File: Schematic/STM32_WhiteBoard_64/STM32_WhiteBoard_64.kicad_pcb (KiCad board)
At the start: 2 copper layers, 25.6 x 60.1 mm, 40 parts, among them J1 SWDIO+Serial, J2 USB_B_Micro, J3 Conn_01x22, J4 Conn_01x22, SW1 Boot0, SW2 Reset, U1 STM32F411RET_Arduino, U2 W25Q32JVSSIQ, U4 NCP1117-3.3_SOT223, X1 ASV-8MHz, Y1 ABS25-32.768KHZ-6-T

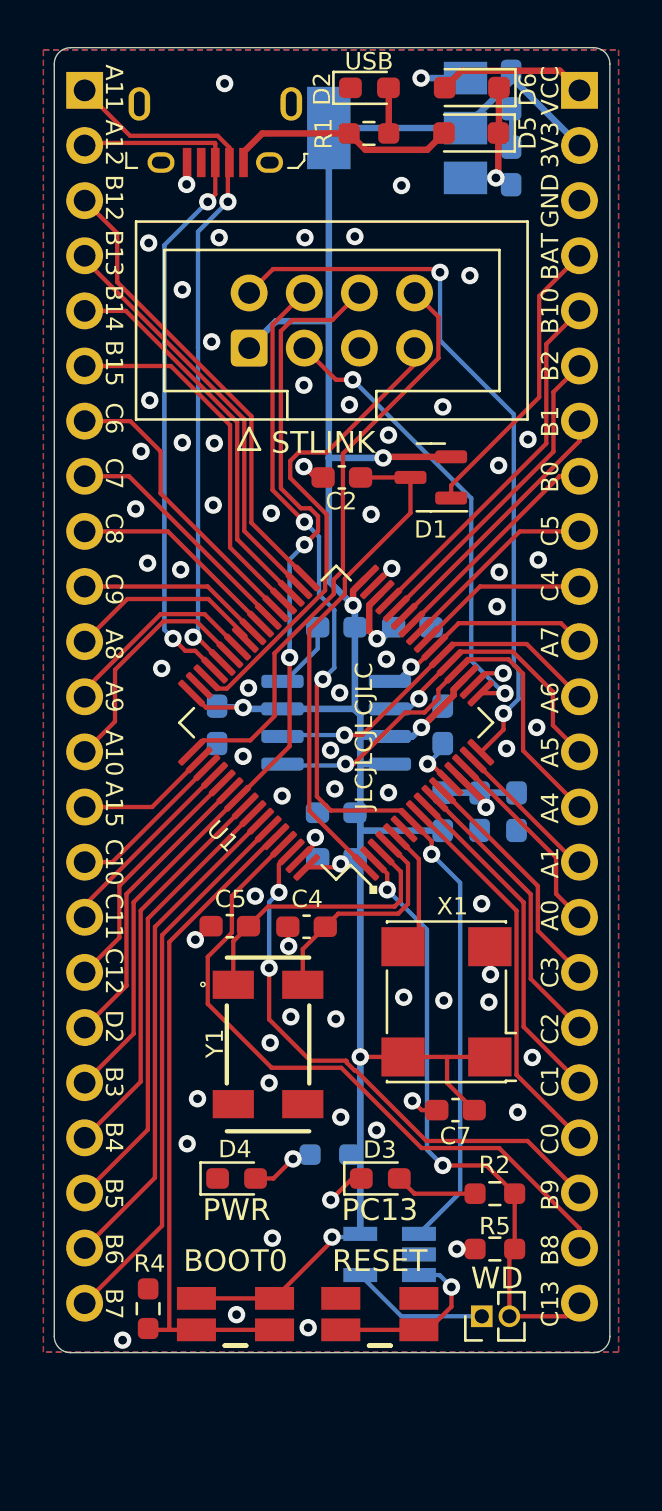
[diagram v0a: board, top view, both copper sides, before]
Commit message: Changed footprints for D6, D7
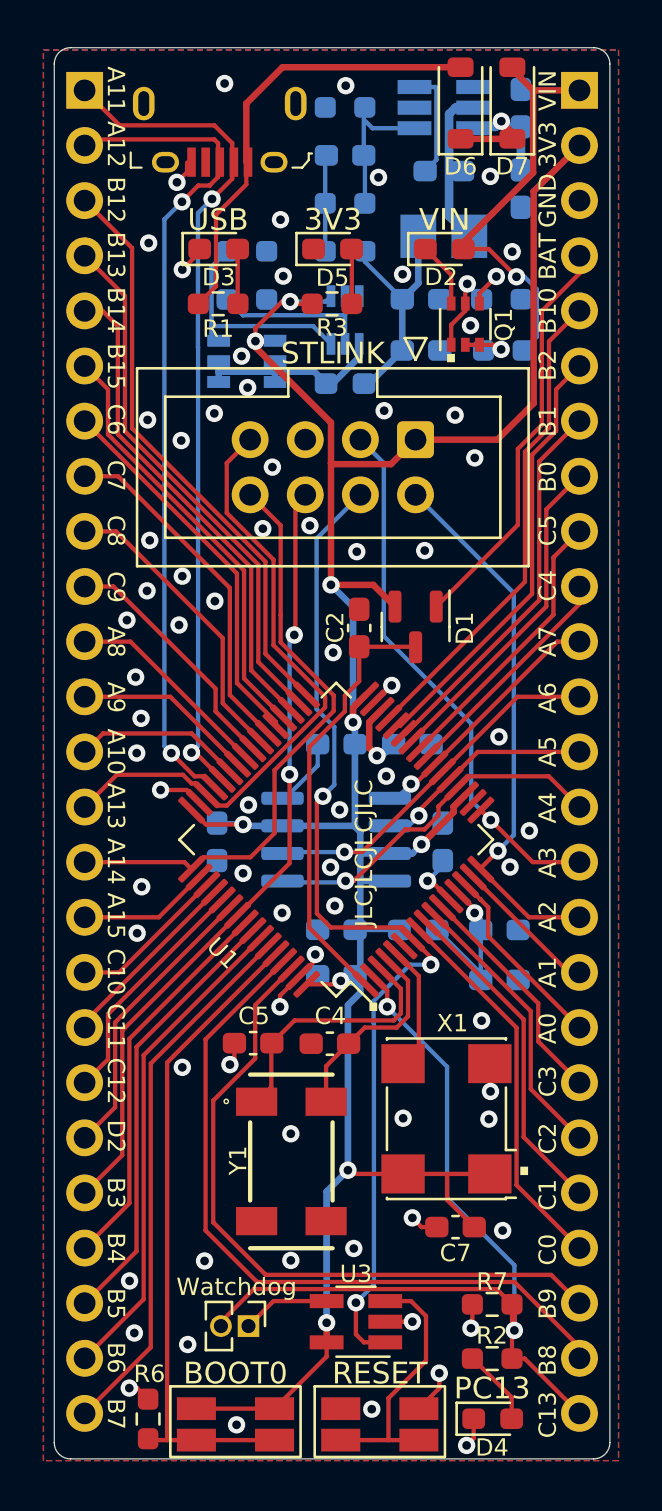
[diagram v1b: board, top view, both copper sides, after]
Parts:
- added C15: 22µF 10V, Capacitor_SMD:C_0603_1608Metric_Pad1.08x0.95mm_HandSolder, B.Cu at (189.9, 90.0)
- added C16: 10µF 35V, Capacitor_SMD:C_0603_1608Metric_Pad1.08x0.95mm_HandSolder, B.Cu at (194.5, 84.9)
- added C17: 100nF, Capacitor_SMD:C_0603_1608Metric_Pad1.08x0.95mm_HandSolder, B.Cu at (194.5, 81.2)
- added C18: 75pF, Capacitor_SMD:C_0603_1608Metric_Pad1.08x0.95mm_HandSolder, B.Cu at (186.4, 83.4)
- added D2: "VIN", LED_SMD:LED_0603_1608Metric_Pad1.05x0.95mm_HandSolder, F.Cu at (191.0, 87.7)
- added FB2: FerriteBead_Small, Inductor_SMD:L_0603_1608Metric_Pad1.05x0.95mm_HandSolder, B.Cu at (186.4, 93.9)
- added L1: 10µH 1A, Inductor_SMD:L_Taiyo-Yuden_NR-20xx_HandSoldering, B.Cu at (190.9, 87.1)
- added Q1: BC847BS, Package_TO_SOT_SMD:SOT-363_SC-70-6, F.Cu at (191.9, 91.1)
- added Q2: Si3493DDV, SamacSys_Parts:SOT95P280X100-6N, B.Cu at (181.9, 92.8)
- added Q3: BC857BS, myDevices:SOT-363_SC-70-6-Handsoldering, B.Cu at (186.4, 91.0)
- added R10: 22kΩ, Resistor_SMD:R_0603_1608Metric_Pad0.98x0.95mm_HandSolder, B.Cu at (186.4, 81.2)
- added R11: 10kΩ, Resistor_SMD:R_0603_1608Metric_Pad0.98x0.95mm_HandSolder, B.Cu at (181.9, 90.0)
- added R12: 10kΩ, Resistor_SMD:R_0603_1608Metric_Pad0.98x0.95mm_HandSolder, B.Cu at (181.9, 87.8)
- added R4: 47kΩ, Resistor_SMD:R_0603_1608Metric_Pad0.98x0.95mm_HandSolder, B.Cu at (193.7, 92.3)
- added R5: 200Ω, Resistor_SMD:R_0603_1608Metric_Pad0.98x0.95mm_HandSolder, B.Cu at (193.6, 90.0)
- added R8: 49.9Ω, Resistor_SMD:R_0603_1608Metric_Pad0.98x0.95mm_HandSolder, B.Cu at (186.4, 87.8)
- added R9: 100kΩ, Resistor_SMD:R_0603_1608Metric_Pad0.98x0.95mm_HandSolder, B.Cu at (186.4, 85.6)
- C13: value 10µF -> 100nF
- C14: value 10µF -> 22µF 10V
- D5: renamed from D4; value "PWR" -> "3V3"
- D6: renamed from D5; footprint Diode_SMD:D_SOD-323_HandSoldering -> Diode_SMD:D_SOD-123
- D7: renamed from D6; footprint Diode_SMD:D_SOD-323_HandSoldering -> Diode_SMD:D_SOD-123
- J3, J4: footprint Connector_PinHeader_2.54mm:PinHeader_1x23_P2.54mm_Vertical -> Connector_PinHeader_2.54mm:PinHeader_1x25_P2.54mm_Vertical
- R3, U3: moved to F.Cu
- U4: value NCP1117-3.3_SOT223 -> TPS54302; footprint Package_TO_SOT_SMD:SOT-223-3_TabPin2 -> Package_TO_SOT_SMD:SOT-23-6_Handsoldering
- moved D5 43.1 mm to (185.8, 87.7)
- moved R3 39.2 mm to (185.8, 90.2)
- moved C14 12.7 mm to (189.9, 92.3), turned to 180 degrees
- moved D4 12.2 mm to (193.2, 141.6)
- moved JP1 10.8 mm to (181.9, 137.3), turned to -90 degrees
- moved R1 10.5 mm to (180.6, 90.2)
- moved D3 10.2 mm to (180.6, 87.7)
- moved J1 8.75 mm to (189.6, 96.5), turned to -90 degrees
- moved C1 7.79 mm to (193.5, 121.3), turned to 180 degrees
- moved R2 7.60 mm to (193.2, 138.8)
- moved C2 6.98 mm to (187.1, 105.1), turned to 90 degrees
- moved D1 6.92 mm to (189.7, 105.1), turned to -90 degrees
- moved FB1 5.56 mm to (189.8, 119.0), turned to 0 degrees
- moved C3 5.53 mm to (193.5, 119.0), turned to 180 degrees
- moved Y1 5.50 mm to (183.9, 129.7)
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- renumbered C11 to C10, C12 to C11, C8 to C12, C9 to C8, C10 to C9, D2 to D3, D3 to D4, R4 to R6, R5 to R7
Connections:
- net /USB_D+ renamed /A12
- net /USB_D- renamed /A11
- net Net-(U3-~{MR}) renamed /~{MR}
- C13 pad 1: Net-(D5-K) -> Net-(U4-SW)
- C13 pad 2: GND -> Net-(U4-BOOT)
- C14 pad 1: +3.3V -> GND
- C14 pad 2: GND -> Net-(C14-Pad2)
- D5 pad 2: Net-(D4-A) (its old number) -> Net-(D5-A)
- D6 pad 1: Net-(D5-K) -> Net-(D6-K)
- D7 pad 1: Net-(D5-K) -> Net-(D6-K)
- J1 pad 2: /STLINK_RX -> /PA2
- J1 pad 3: /STLINK_TX -> /PA3
- J1 pad 7: /STLINK_SWDIO -> /PA13
- J1 pad 8: /SWCLK -> /PA14
- J3 pad 15: /PA1 -> /PA3
- J3 pad 16: /PA0 -> /PA2
- J3 pad 17: /PC3 -> /PA1
- J3 pad 18: /PC2 -> /PA0
- J3 pad 19: /PC1 -> /PC3
- J3 pad 20: /PC0 -> /PC2
- J3 pad 21: /PB9 -> /PC1
- J3 pad 22: /PB8 -> /PC0
- J3 pad 23: /PC13 -> /PB9
- J4 pad 14: /PA15 -> /PA13
- J4 pad 15: /PC10 -> /PA14
- J4 pad 16: /PC11 -> /PA15
- J4 pad 17: /PC12 -> /PC10
- J4 pad 18: /PD2 -> /PC11
- J4 pad 19: /PB3 -> /PC12
- J4 pad 20: /PB4 -> /PD2
- J4 pad 21: /PB5 -> /PB3
- J4 pad 22: /PB6 -> /PB4
- J4 pad 23: /PB7 -> /PB5
- R3 pad 1: +3.3V -> Net-(D5-A)
- R3 pad 2: Net-(D4-A) (its old number) -> +3.3V
- U1 pad 16: /STLINK_RX -> /PA2
- U1 pad 17: /STLINK_TX -> /PA3
- U1 pad 46: /STLINK_SWDIO -> /PA13
- U1 pad 49: /SWCLK -> /PA14
- U4 pad 2: +3.3V -> Net-(U4-SW)
- U4 pad 3: Net-(D5-K) -> Net-(D6-K)
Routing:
- net /STLINK_RX: track 33.7 -> 0.00 mm, vias 2 -> 0
- net /PA13: track 0.00 -> 28.8 mm
- net /PA14: track 0.00 -> 27.9 mm
- net /SWCLK: track 27.6 -> 0.00 mm
- net /PA3: track 0.00 -> 25.6 mm, vias 0 -> 1
- net /PA2: track 0.00 -> 25.2 mm, vias 0 -> 1
- net /STLINK_SWDIO: track 22.5 -> 0.00 mm
- net /STLINK_TX: track 21.3 -> 0.00 mm, vias 2 -> 0
- net /PC13: track 28.5 -> 41.4 mm
- net VCC: track 6.91 -> 19.2 mm, vias 0 -> 1
- net Net-(C14-Pad2): track 0.00 -> 10.9 mm
- net Net-(Q2-G): track 0.00 -> 10.4 mm
- net VBUS: track 10.7 -> 20.7 mm
- net Net-(Q3A-E1): track 0.00 -> 9.71 mm
- net Net-(Q3A-B1): track 0.00 -> 8.60 mm
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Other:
- board size 25.6 x 60.1 mm -> 25.6 x 65 mm
- board text added: "A13"
- board text added: "A14"
- board text added: "A2"
- board text added: "A3"
- board text added: "STM32_WhiteBoard_64 R0144_2334_Pb Bjørner Sandom"
- board text added: "VIN"
- board text added: "Watchdog"
- board text removed: "PWR"
- board text removed: "STM32F411RET6 {dblquote}Whiteboard{dblquote} R0102B_2334_Pb Bjørner Sandom"
- board text removed: "VCC"
- board text removed: "WD"

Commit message: Updated symbols
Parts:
- J3: value Conn_01x22 -> Header1
- J4: value Conn_01x22 -> Header2
- U1: value STM32F411RET_Arduino -> STM32F411RET6
- U3: value ~ -> TPS3828-33DBVR
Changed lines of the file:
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@@
         (effects (font (size 0.8 0.8) (thickness 0.1)))
     )
-    (fp_text value "~" (at 0 2.9) (layer "F.Fab")
+    (fp_text value "TPS3828-33DBVR" (at 0 2.9) (layer "F.Fab")
         (effects (font (size 1 1) (thickness 0.15)))
     )
@@
     (descr "ABS25")
     (tags "Crystal or Oscillator")
+    (property "Comments" "")
     (property "Description" "32.768 kHz LOW FREQUENCY SMD CRYSTAL")
     (property "Height" "")
@@
     (descr "Miniature Crystal Clock Oscillator Abracon ASV series, http://www.abracon.com/Oscillators/ASV.pdf, 7.0x5.1mm^2 package")
     (tags "SMD SMT crystal oscillator")
+    (property "Comments" "")
     (property "Sheetfile" "STM32_WhiteBoard_64.kicad_sch")
     (property "Sheetname" "")
@@
     (descr "LQFP, 64 Pin (https://www.analog.com/media/en/technical-documentation/data-sheets/ad7606_7606-6_7606-4.pdf), generated with kicad-footprint-generator ipc_gullwing_generator.py")
     (tags "LQFP QFP")
+    (property "Comments" "")
     (property "Sheetfile" "STM32_WhiteBoard_64.kicad_sch")
     (property "Sheetname" "")
@@
         (effects (font (size 0.8 0.8) (thickness 0.1)))
     )
-    (fp_text value "STM32F411RET_Arduino" (at 0 7.4 135) (layer "F.Fab") hide
+    (fp_text value "STM32F411RET6" (at 0 7.4 135) (layer "F.Fab") hide
         (effects (font (size 1 1) (thickness 0.15)))
     )
@@
         (effects (font (size 0.8 0.8) (thickness 0.1)) (justify mirror))
     )
-    (fp_text value "Conn_01x22" (at 0 -63.29) (layer "B.Fab")
+    (fp_text value "Header2" (at 0 -63.29) (layer "B.Fab")
         (effects (font (size 1 1) (thickness 0.15)) (justify mirror))
     )
@@
         (effects (font (size 0.8 0.8) (thickness 0.1)) (justify mirror))
     )
-    (fp_text value "Conn_01x22" (at 0 -63.29) (layer "B.Fab")
+    (fp_text value "Header1" (at 0 -63.29) (layer "B.Fab")
         (effects (font (size 1 1) (thickness 0.15)) (justify mirror))
     )
@@
     (descr "SOT-363, SC-70-6")
     (tags "SOT-363 SC-70-6")
+    (property "Comments" "")
     (property "Sheetfile" "STM32_WhiteBoard_64.kicad_sch")
     (property "Sheetname" "")
@@
     (descr "SOIC, 8 Pin (JEDEC MS-012AA, https://www.analog.com/media/en/package-pcb-resources/package/pkg_pdf/soic_narrow-r/r_8.pdf), generated with kicad-footprint-generator ipc_gullwing_generator.py")
     (tags "SOIC SO")
+    (property "Comments" "")
     (property "Sheetfile" "STM32_WhiteBoard_64.kicad_sch")
     (property "Sheetname" "")
@@
     (descr "6-pin SOT-23 package, Handsoldering")
     (tags "SOT-23-6 Handsoldering")
-    (property "Sheetfile" "STM32_WhiteBoard_64.kicad_sch")
-    (property "Sheetname" "")
+    (property "Comments" "")
+    (property "Sheetfile" "STM32_WhiteBoard_64.kicad_sch")
+    (property "Sheetname" "")

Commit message: Changed component value
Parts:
- R1: value 560Ω -> 1kΩ
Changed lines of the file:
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@@
         (effects (font (size 0.8 0.8) (thickness 0.1)))
     )
-    (fp_text value "560Ω" (at 0 1.43) (layer "F.Fab")
+    (fp_text value "1kΩ" (at 0 1.43) (layer "F.Fab")
         (effects (font (size 1 1) (thickness 0.15)))
     )
